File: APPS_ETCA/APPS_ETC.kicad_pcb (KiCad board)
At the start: 2 copper layers, 81.3 x 86.4 mm, 27 parts, among them P1 DTM1312PC12PDR008, U1 NUCLEO-L432KC, U2 MCP6004, U6 LM7805_TO220, U8 LM7809_TO220

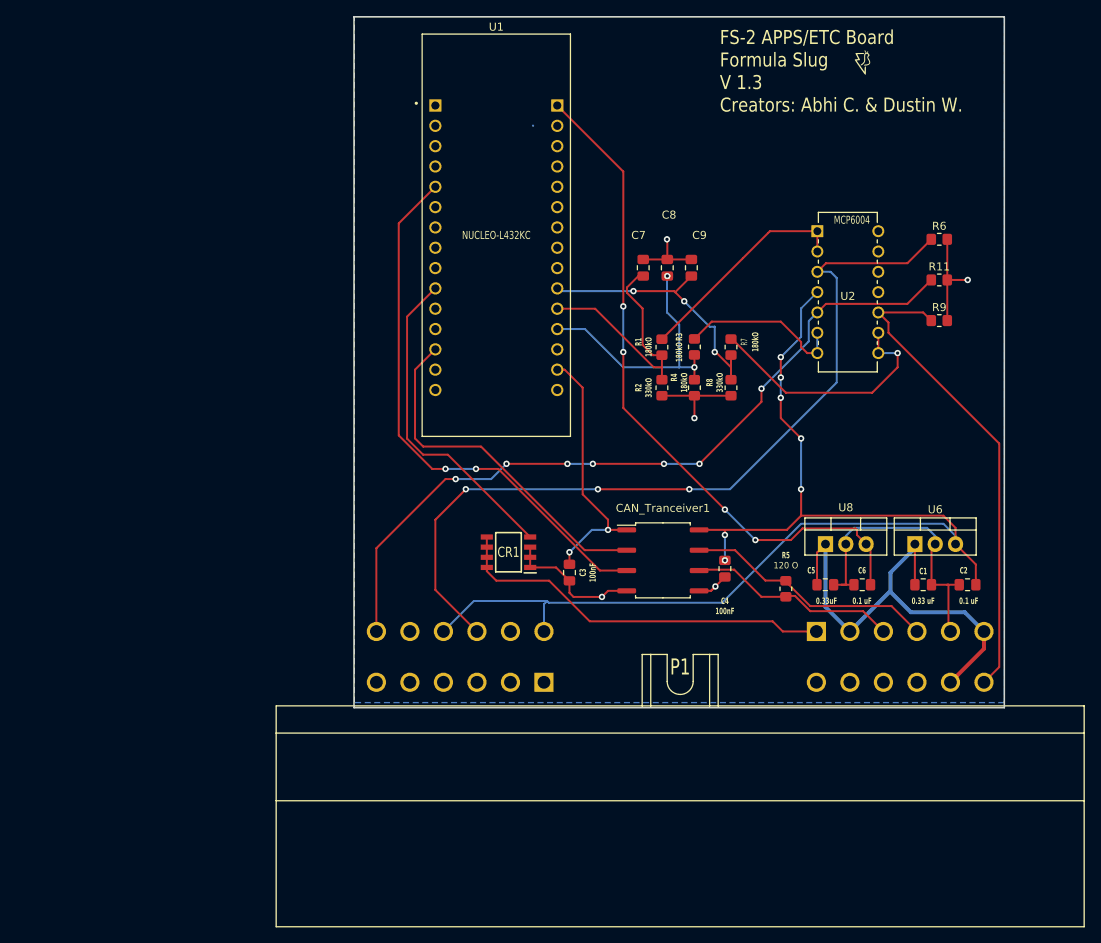
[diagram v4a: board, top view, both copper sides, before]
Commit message: cockpit in, rtds control, and 3.3v and organized.
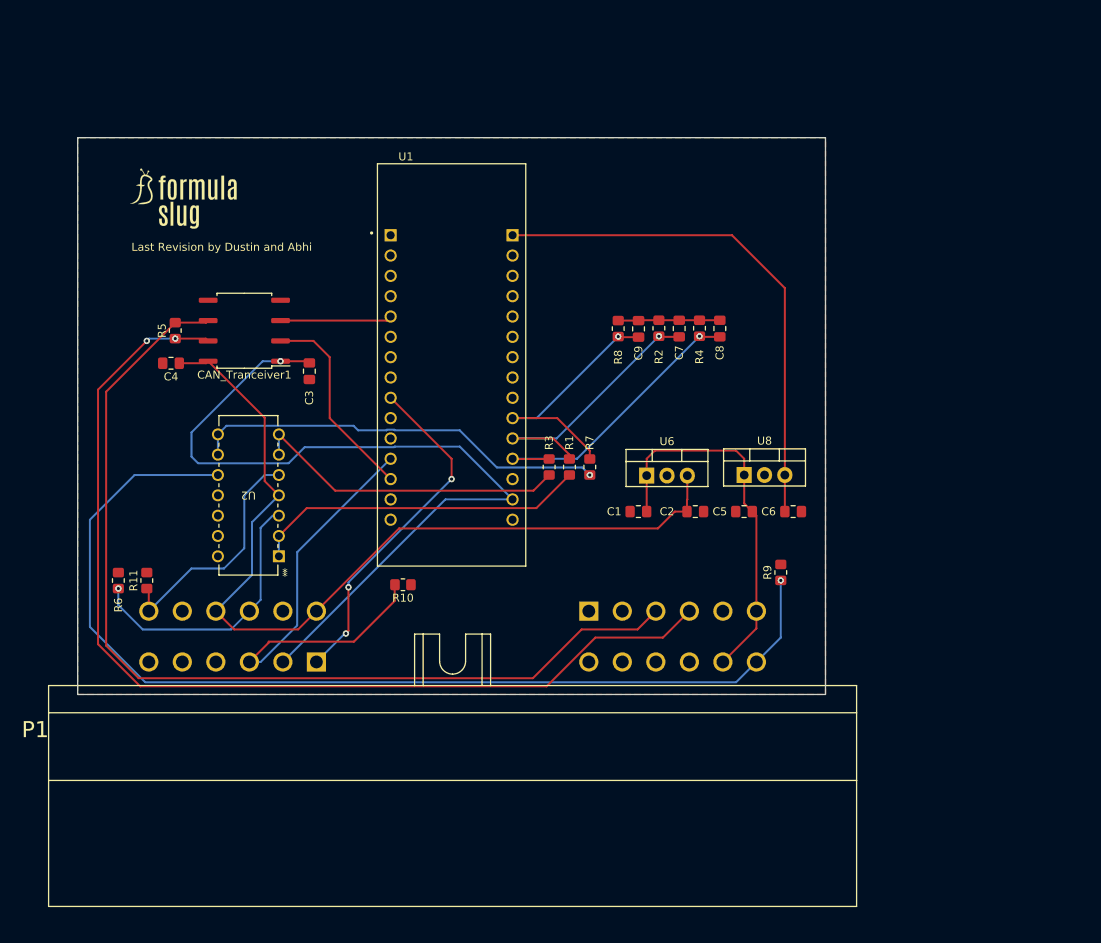
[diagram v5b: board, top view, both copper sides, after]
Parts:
- removed CR1: STS6NF20V, 1FS_2_Global_Footprint_Library:SOIC127P600X175-8N
- removed FS-2 APPS/ETC Board: LOGO, 1FS_2_Global_Footprint_Library:FORMULA SLUG
- added G***: LOGO, FSFootprints:FS_Logo, F.Cu at (147.9, 71.7)
- added R10: 100k, Resistor_SMD:R_0805_2012Metric_Pad1.20x1.40mm_HandSolder, F.Cu at (176.3, 119.9)
- C1: value 0.33 uF -> 0.33 mF
- C2, C6: value 0.1 uF -> 0.1 mF
- C5: value 0.33uF -> 0.33mF
- C7, C8: value .047 uF -> 40 nF
- C9: value .047 uf -> 40 nF
- P1: footprint 1FS_2_Global_Footprint_Library:TE_DTM1312PC12PDR008 -> FSFootprints:TE_DTM1312PC12PDR008
- moved R6 111.1 mm to (140.7, 119.4), turned to 90 degrees
- moved R11 105.9 mm to (144.3, 119.4), turned to 90 degrees
- moved R5 82.9 mm to (147.8, 88.1), turned to 90 degrees
- moved U2 78.6 mm to (160.8, 116.3), turned to 180 degrees
- moved C4 73.8 mm to (147.3, 92.2), turned to 180 degrees
- moved CAN_Tranceiver1 59.7 mm to (156.5, 88.1), turned to 180 degrees
- moved C3 41.1 mm to (164.6, 93.2)
- moved R9 37.2 mm to (223.5, 118.3), turned to 90 degrees
- moved C1 36.8 mm to (205.7, 110.7), turned to 180 degrees
- moved C2 35.2 mm to (212.8, 110.7), turned to 0 degrees
- moved U6 34.6 mm to (206.8, 106.2)
- moved P1 28.6 mm to (182.5, 127.6)
- moved R3 23.6 mm to (194.6, 105.2), turned to 90 degrees
- moved R7 23.2 mm to (199.6, 105.2), turned to 90 degrees
- moved R1 18.9 mm to (197.1, 105.2), turned to 90 degrees
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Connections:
- P1 pad C1: unconnected-(P1-PadC1) -> /RTDS Control
- P1 pad C2: unconnected-(P1-PadC2) -> +3.3V
- P1 pad C3: unconnected-(P1-PadC3) -> /Cockpit In
- P1 pad D2: +12V -> /RTDS Power
- U1 pad CN3_10: /RTDS Control -> unconnected-(U1A-D7-PadCN3_10)
- U1 pad CN3_12: unconnected-(U1A-PA8-PadCN3_12) -> /Cockpit In
- U1 pad CN3_9: unconnected-(U1A-PB1-PadCN3_9) -> /RTDS Control
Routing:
- net /CANH: track 31.4 -> 128.3 mm, vias 0 -> 2
- net /CANL: track 27.0 -> 122.0 mm
- net GND: track 91.8 -> 12.7 mm, vias 5 -> 0
- net /OUT1: track 105.1 -> 34.6 mm, vias 3 -> 1
- net /Brake Sensor: track 60.3 -> 130.4 mm, vias 0 -> 1
- net +3.3V: track 33.0 -> 102.7 mm, vias 2 -> 1
- net /OUT2: track 96.1 -> 30.1 mm, vias 7 -> 0
- net /Cockpit In: track 0.00 -> 57.0 mm
- net /D2 OUT: track 68.5 -> 14.0 mm, vias 2 -> 0
- net /RTDS GND: track 48.6 -> 0.00 mm
- net +5V: track 151.7 -> 112.3 mm, vias 7 -> 0
- net +9V: track 85.5 -> 64.7 mm, vias 4 -> 0
- net Net-(U2C--): track 31.8 -> 52.1 mm
- net Net-(U2B--): track 20.8 -> 40.0 mm
- net /D10 OUT: track 44.4 -> 25.4 mm
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- added copper zone on F.Cu, net GND
- removed copper zone on B.Cu, net GND
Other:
- board size 81.3 x 86.4 mm -> 93.5 x 69.6 mm
- board text added: "Last Revision by Dustin and Abhi"
- board text removed: "FS-2 APPS/ETC Board Formula Slug V 1.3 Creators: Abhi C. & Dustin W."

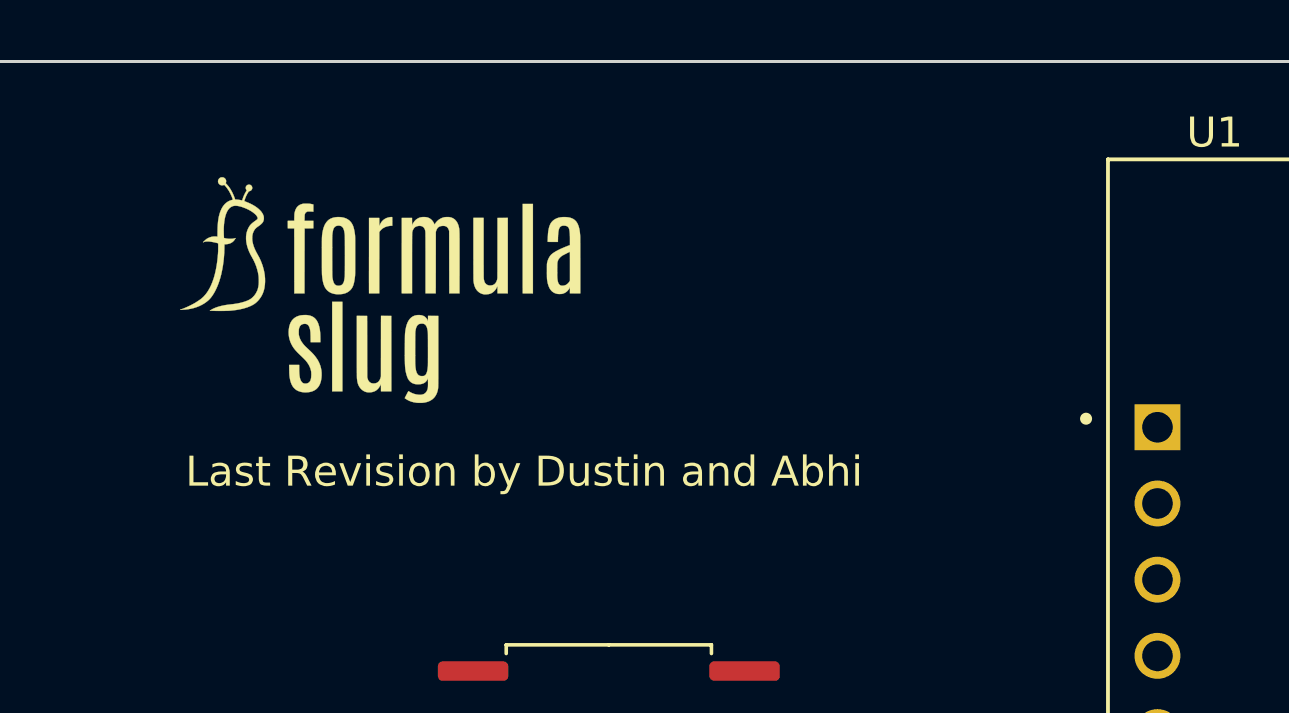
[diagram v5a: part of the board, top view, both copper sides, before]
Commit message: Added some more information on the silkscreen
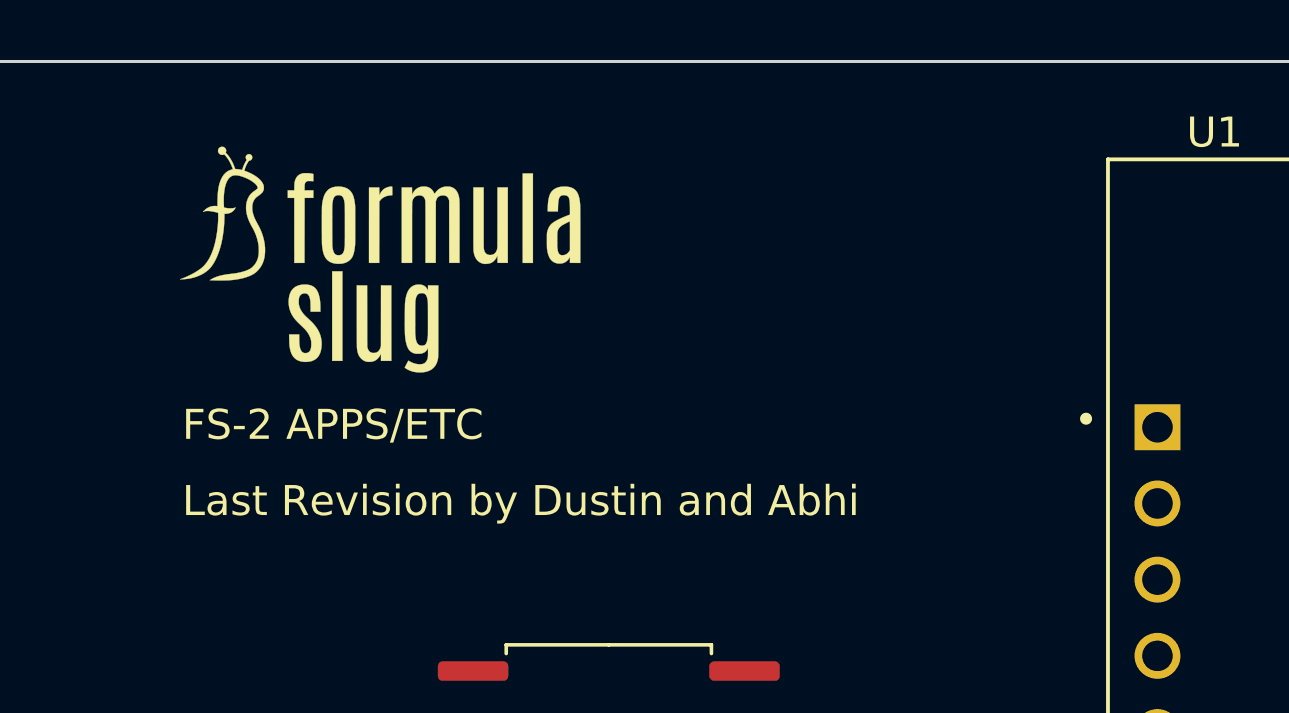
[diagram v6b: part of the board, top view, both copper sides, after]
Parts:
- moved G*** 1.02 mm to (147.9, 70.6)
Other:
- board text added: "FS-2 APPS/ETC"
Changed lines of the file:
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@@
   )
   (footprint "FSFootprints:FS_Logo" (layer "F.Cu")
-    (at 147.936859 71.664981)
+    (at 147.936859 70.648981)
     (attr through_hole)
     (fp_text reference "G***" (at 0 0) (layer "F.SilkS") hide
@@
   (gr_rect (start 135.636 64.008) (end 229.108 133.604)
     (stroke (width 0.1) (type default)) (fill none) (layer "Edge.Cuts"))
-  (gr_text "Last Revision by Dustin and Abhi" (at 142.348859 78.268981) (layer "F.SilkS")
+  (gr_text "FS-2 APPS/ETC" (at 142.24 76.708) (layer "F.SilkS")
+    (effects (font (size 1 1) (thickness 0.15)) (justify left bottom))
+  )
+  (gr_text "Last Revision by Dustin and Abhi" (at 142.24 79.248) (layer "F.SilkS")
     (effects (font (size 1 1) (thickness 0.15)) (justify left bottom))
   )
